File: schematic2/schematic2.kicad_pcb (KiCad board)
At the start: 2 copper layers, 69.2 x 56 mm, 36 parts, among them J1 Barrel_Jack, K1 TIANBO_HJR_1-2C, P1 Conn_02x20_Odd_Even, Q1 BC547, Q2 BC557, Q3 BC547, Q4 BC547, U1 buck

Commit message: modified:   schematic2/schematic2.kicad_pcb new file:   schematic2/schematic2.pro modified:   schematic2/schematic2.sch
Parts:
- added J2: I2C BUS, Connector_Molex:Molex_KK-254_AE-6410-05A_1x05_P2.54mm_Vertical, F.Cu at (218.5, 103.2)
- added REF**: KiCad-Logo_6mm_SilkScreen, Symbol:KiCad-Logo_6mm_SilkScreen, F.Cu at (262.0, 133.5)
- BT1: value 6x AA NiMh -> 6x AAA NiMh
- D11: value LED -> PWR
- D8: value LED -> PWR_FAIL
- R3: value 82R -> 120R
- moved D11 27.7 mm to (206.2, 131.5), turned to 90 degrees
- moved R11 15.6 mm to (206.2, 126.2), turned to 90 degrees
- moved U1 8.50 mm to (259.2, 114.0)
- moved K1 7.75 mm to (228.2, 112.8)
- moved R9 4.50 mm to (223.5, 107.2)
- moved R10 4.25 mm to (223.5, 109.5)
- moved Q4 4.03 mm to (214.0, 110.5)
- moved J1 0.50 mm to (252.5, 135.8)
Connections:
- D10 pad 2: +3V3 -> PI_P_SIG
- P1 pad 1: (no net) -> Net-(J2-Pad5)
- P1 pad 13: (no net) -> PI_P_SIG
- P1 pad 17: +3V3 -> (no net)
- P1 pad 3: (no net) -> /GPIO2(SDA1)
- P1 pad 5: (no net) -> /GPIO3(SCL1)
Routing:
- net PI_P_SIG: track 0.00 -> 16.2 mm
- net +5V: track 90.0 -> 105.1 mm
- net +3V3: track 10.6 -> 0.00 mm
- net Net-(D9-Pad2): track 10.2 -> 15.4 mm
- net Net-(D7-Pad1): track 29.9 -> 35.0 mm
- net Net-(J2-Pad5): track 0.00 -> 4.49 mm
- net GND: track 0.00 -> 4.49 mm
- net /GPIO3(SCL1): track 0.00 -> 4.49 mm
- net /GPIO2(SDA1): track 0.00 -> 4.49 mm
- net Net-(D5-Pad1): track 12.5 -> 16.5 mm
- net Net-(D11-Pad2): track 6.00 -> 2.75 mm
- net Net-(D10-Pad1): track 8.08 -> 10.3 mm
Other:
- board size 69.2 x 56 mm -> 68.8 x 56 mm
- board text added: "(C) Mike Evans 2018"
- board text added: "+"
- board text removed: "RASPBERRY-PI 40-PIN ADDON BOARD VIEW FROM TOP NOTE: P1 SHOULD BE FITTED ON THE REVERSE OF THE BOARD ADD EDGE CUTS FROM CAMERA AND DISPLAY PORTS AS REQUIRED"

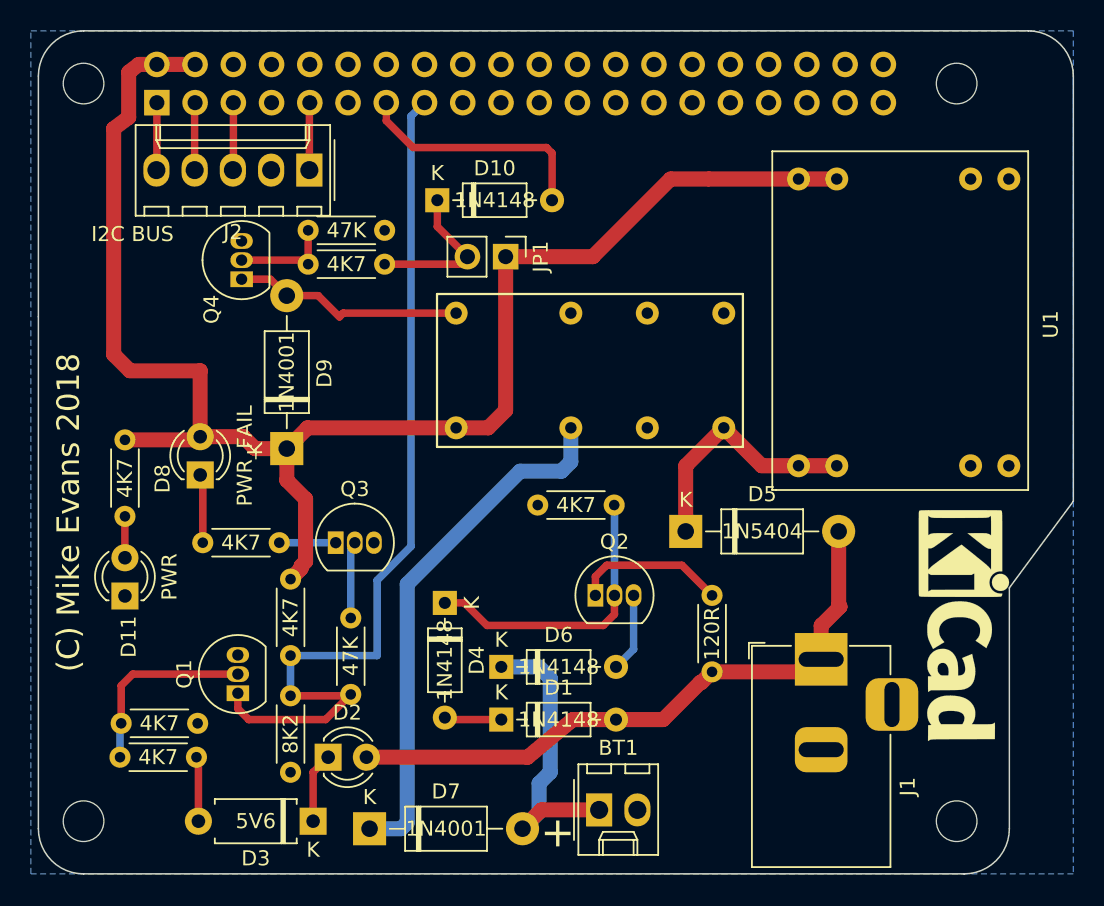
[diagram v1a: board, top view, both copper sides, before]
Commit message: add fuse and logo.
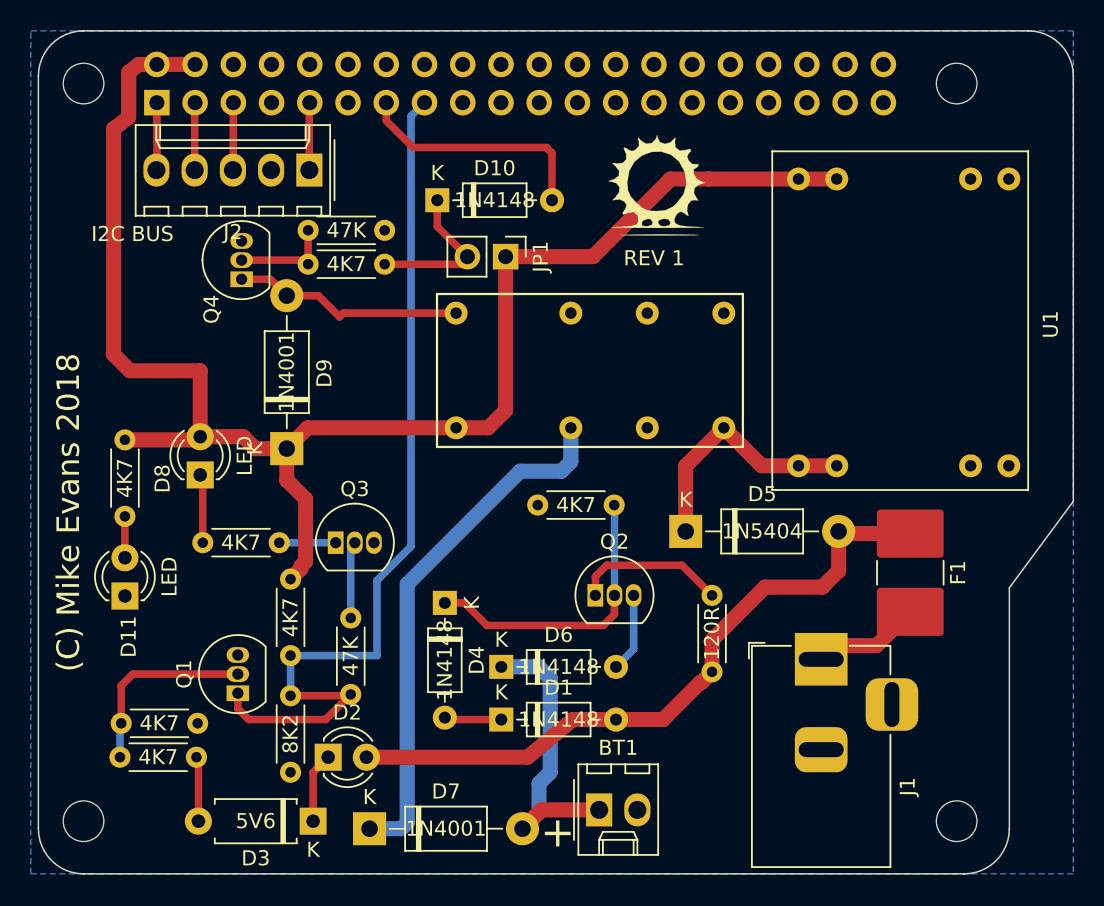
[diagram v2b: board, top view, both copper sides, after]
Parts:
- removed REF**: KiCad-Logo_6mm_SilkScreen, Symbol:KiCad-Logo_6mm_SilkScreen
- added F1: Polyfuse, Fuse:Fuse_2816_7142Metric_Pad3.20x4.45mm_HandSolder, F.Cu at (258.4, 130.0)
- added G***: LOGO, Mikee:MS_LOGO, F.Cu at (241.7, 104.3)
- D11: value PWR -> LED
- D8: value PWR_FAIL -> LED
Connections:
- J1 pad 1: +9V -> Net-(F1-Pad2)
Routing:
- net Net-(F1-Pad2): track 0.00 -> 7.76 mm
- net +9V: track 42.1 -> 45.0 mm
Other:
- board text added: "REV 1"

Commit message: Change clock for discreets.
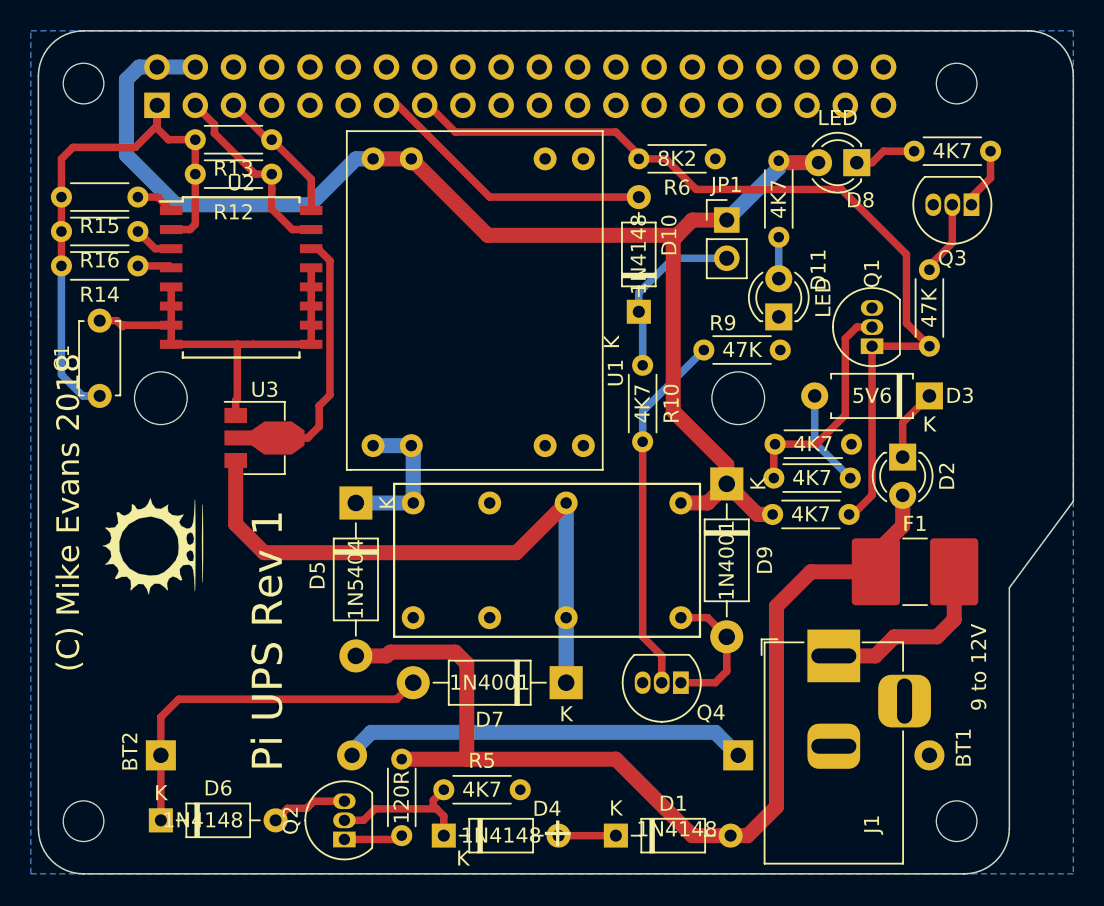
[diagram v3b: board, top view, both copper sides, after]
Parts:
- removed J2: I2C BUS, Connector_Molex:Molex_KK-254_AE-6410-05A_1x05_P2.54mm_Vertical
- added BT2: 3x AAA NiMh, Battery:BatteryHolder_Keystone_2479_3xAAA, F.Cu at (208.6, 142.1)
- added C1: C_Small, Capacitor_THT:C_Disc_D4.7mm_W2.5mm_P5.00mm, F.Cu at (204.6, 118.2)
- added R12: 4K7, Resistor_THT:R_Axial_DIN0204_L3.6mm_D1.6mm_P5.08mm_Horizontal, F.Cu at (216.0, 103.5)
- added R13: 4K7, Resistor_THT:R_Axial_DIN0204_L3.6mm_D1.6mm_P5.08mm_Horizontal, F.Cu at (216.0, 101.2)
- added R14: 4K7, Resistor_THT:R_Axial_DIN0204_L3.6mm_D1.6mm_P5.08mm_Horizontal, F.Cu at (207.1, 109.6)
- added R15: 4K7, Resistor_THT:R_Axial_DIN0204_L3.6mm_D1.6mm_P5.08mm_Horizontal, F.Cu at (207.1, 105.0)
- added R16: 4K7, Resistor_THT:R_Axial_DIN0204_L3.6mm_D1.6mm_P5.08mm_Horizontal, F.Cu at (207.1, 107.3)
- added U2: DS3231M, Package_SO:SOIC-16W_7.5x10.3mm_P1.27mm, F.Cu at (214.0, 110.4)
- added U3: MCP1700-1202E_SOT89, Package_TO_SOT_SMD:SOT-89-3, F.Cu at (215.1, 121.0)
- BT1: value 6x AAA NiMh -> 3x AAA NiMh; footprint Connector_Molex:Molex_KK-254_AE-6410-02A_1x02_P2.54mm_Vertical -> Battery:BatteryHolder_Keystone_2479_3xAAA
- moved R8 53.9 mm to (263.8, 102.0)
- moved D3 49.7 mm to (259.7, 118.2)
- moved R6 49.6 mm to (245.5, 102.5), turned to 180 degrees
- moved D8 48.3 mm to (254.9, 102.8), turned to 180 degrees
- moved Q1 48.0 mm to (255.9, 114.9)
- moved Q3 47.8 mm to (262.5, 105.5), turned to 180 degrees
- moved D11 47.2 mm to (249.7, 113.0)
- moved R1 47.2 mm to (254.4, 123.7)
- moved R11 47.2 mm to (249.7, 107.7)
- moved R2 47.2 mm to (249.4, 121.5)
- moved R7 44.9 mm to (259.7, 109.9)
- moved D2 43.1 mm to (257.9, 122.3), turned to 270 degrees
- moved G*** 41.2 mm to (208.1, 128.2), turned to 90 degrees
- moved Q4 39.6 mm to (243.2, 137.3), turned to 180 degrees
- moved R4 38.3 mm to (254.4, 126.1), turned to 180 degrees
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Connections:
- D6 pad 1: Net-(BT1-Pad1) -> Net-(BT2-Pad1)
- D7 pad 2: Net-(BT1-Pad1) -> Net-(BT2-Pad1)
- K1 pad 4: (no net) -> Net-(D7-Pad1)
- P1 pad 1: Net-(J2-Pad5) -> +3V3
- P1 pad 3: /GPIO2(SDA1) -> SDA1
- P1 pad 5: /GPIO3(SCL1) -> SCL1
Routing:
- net +3V3: track 0.00 -> 37.9 mm
- net Net-(BT2-Pad1): track 0.00 -> 24.6 mm
- net +9V: track 45.0 -> 68.6 mm
- net GND: track 4.49 -> 27.9 mm
- net Net-(U2-Pad14): track 0.00 -> 18.6 mm
- net Net-(Q4-Pad2): track 6.78 -> 24.3 mm
- net +5V: track 105.1 -> 88.6 mm
- net SDA1: track 0.00 -> 12.9 mm
- net Net-(D4-Pad1): track 19.5 -> 10.1 mm
- net SCL1: track 0.00 -> 9.33 mm
- net Net-(BT1-Pad1): track 19.9 -> 27.1 mm
- net Net-(D5-Pad1): track 16.5 -> 10.2 mm
- net Net-(Q2-Pad1): track 10.1 -> 3.92 mm
- net Net-(D9-Pad2): track 15.4 -> 9.22 mm
- net Net-(D7-Pad1): track 35.0 -> 40.3 mm
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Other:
- board text added: "9 to 12V"
- board text added: "Pi UPS Rev 1"
- board text removed: "REV 1"

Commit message: Layout done.
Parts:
- added C2: CP, Capacitor_THT:C_Disc_D4.7mm_W2.5mm_P5.00mm, F.Cu at (225.4, 120.7)
- added C3: C_Small, Capacitor_THT:C_Disc_D4.7mm_W2.5mm_P5.00mm, F.Cu at (233.4, 108.0)
- added C4: CP, Capacitor_THT:C_Disc_D4.7mm_W2.5mm_P5.00mm, F.Cu at (237.1, 107.8)
- added D12: D_Zener, Diode_THT:D_DO-35_SOD27_P7.62mm_Horizontal, F.Cu at (230.7, 122.6)
- added L1: INDUCTOR, Inductor_SMD:L_7.3x7.3_H3.5, F.Cu at (234.3, 117.2)
- added R17: R, Resistor_THT:R_Axial_DIN0204_L3.6mm_D1.6mm_P5.08mm_Horizontal, F.Cu at (221.8, 111.6)
- added R18: R, Resistor_THT:R_Axial_DIN0204_L3.6mm_D1.6mm_P5.08mm_Horizontal, F.Cu at (224.6, 104.8)
- added R19: R, Resistor_THT:R_Axial_DIN0204_L3.6mm_D1.6mm_P5.08mm_Horizontal, F.Cu at (237.3, 111.9)
- U1: value buck -> MC34063AD; footprint Mikee:BUCK_MODULE_5V -> Package_SO:SOIC-8_3.9x4.9mm_P1.27mm
- moved U1 5.24 mm to (226.9, 109.4), turned to 180 degrees
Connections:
- D5 pad 1: Net-(D5-Pad1) -> /Sheet5B480DB4/Vin
- K1 pad 9: Net-(D5-Pad1) -> /Sheet5B480DB4/Vin
- U1 pad 1: Net-(D5-Pad1) -> Net-(R17-Pad1)
- U1 pad 2: GND -> Net-(D12-Pad1)
- U1 pad 3: GND -> Net-(C3-Pad1)
- U1 pad 4: +5V -> GND
- U3 pad 3: Net-(D7-Pad1) -> (no net)
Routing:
- net /Sheet5B480DB4/Vin: track 0.00 -> 28.0 mm
- net Net-(R17-Pad1): track 0.00 -> 27.6 mm
- net Net-(D12-Pad1): track 0.00 -> 18.2 mm
- net Net-(R18-Pad1): track 0.00 -> 15.7 mm
- net +5V: track 88.6 -> 99.5 mm
- net Net-(D5-Pad1): track 10.2 -> 0.00 mm
- net Net-(D7-Pad1): track 40.3 -> 36.0 mm
- net Net-(C3-Pad1): track 0.00 -> 4.09 mm
- net GND: track 27.9 -> 30.1 mm

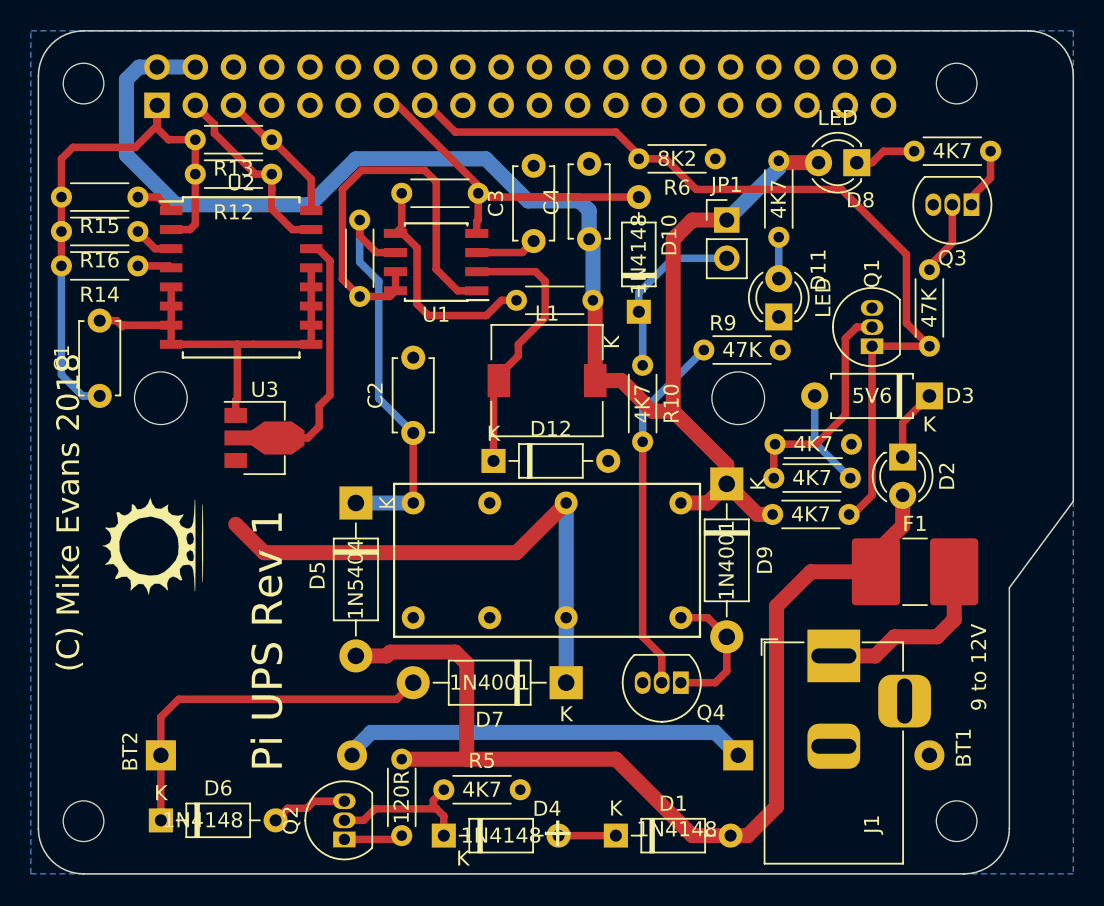
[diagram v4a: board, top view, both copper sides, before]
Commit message: Put the prebuilt buck converter back.
It's cheaper and easier.
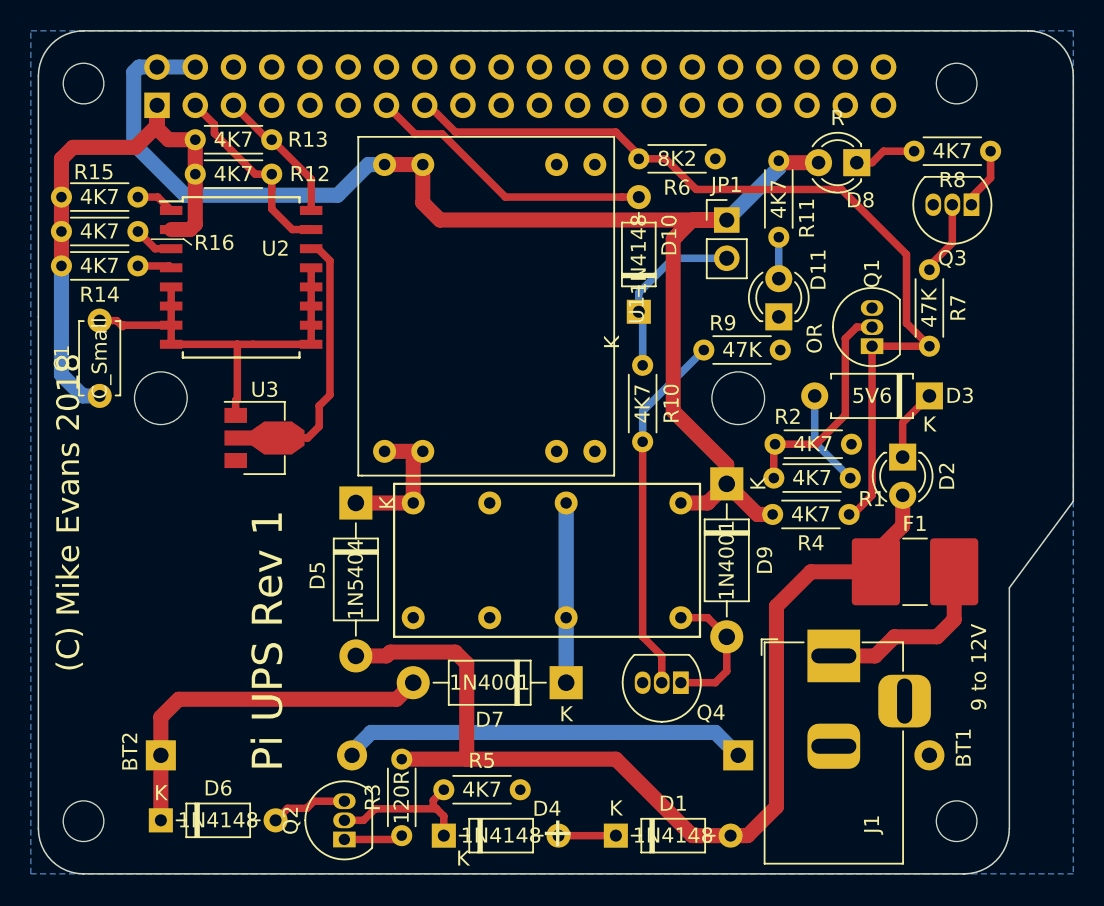
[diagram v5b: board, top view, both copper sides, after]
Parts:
- removed C2, C4: CP, Capacitor_THT:C_Disc_D4.7mm_W2.5mm_P5.00mm
- removed C3: C_Small, Capacitor_THT:C_Disc_D4.7mm_W2.5mm_P5.00mm
- removed D12: D_Zener, Diode_THT:D_DO-35_SOD27_P7.62mm_Horizontal
- removed G***: LOGO, Mikee:MS_LOGO
- removed L1: INDUCTOR, Inductor_SMD:L_7.3x7.3_H3.5
- removed R17, R18, R19: R, Resistor_THT:R_Axial_DIN0204_L3.6mm_D1.6mm_P5.08mm_Horizontal
- D11: value LED -> OR
- D2: value LED -> G
- D8: value LED -> R
- U1: value MC34063AD -> buck; footprint Package_SO:SOIC-8_3.9x4.9mm_P1.27mm -> Mikee:BUCK_MODULE_5V
- moved U1 6.07 mm to (231.8, 113.0), turned to 90 degrees
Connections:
- D5 pad 1: /Sheet5B480DB4/Vin -> Net-(D5-Pad1)
- K1 pad 11: (no net) -> Net-(K1-Pad11)
- K1 pad 6: (no net) -> Net-(K1-Pad6)
- K1 pad 8: (no net) -> Net-(K1-Pad8)
- K1 pad 9: /Sheet5B480DB4/Vin -> Net-(D5-Pad1)
- P1 pad 10: (no net) -> /GPIO15(RXD0)
- P1 pad 11: (no net) -> /GPIO17(GEN0)
- P1 pad 12: (no net) -> /GPIO18(GEN1)(PWM0)
- P1 pad 16: (no net) -> /GPIO23(GEN4)
- P1 pad 17: (no net) -> Net-(P1-Pad17)
- P1 pad 18: (no net) -> /GPIO24(GEN5)
- P1 pad 19: (no net) -> /GPIO10(SPI0_MOSI)
- P1 pad 21: (no net) -> /GPIO9(SPI0_MISO)
- P1 pad 22: (no net) -> /GPIO25(GEN6)
- P1 pad 23: (no net) -> /GPIO11(SPI0_SCK)
- P1 pad 24: (no net) -> /GPIO8(SPI0_CE_N)
- P1 pad 26: (no net) -> /GPIO7(SPI1_CE_N)
- P1 pad 27: (no net) -> /ID_SD
- P1 pad 28: (no net) -> /ID_SC
- P1 pad 29: (no net) -> /GPIO5
- P1 pad 31: (no net) -> /GPIO6
- P1 pad 32: (no net) -> /GPIO12(PWM0)
- P1 pad 33: (no net) -> /GPIO13(PWM1)
- P1 pad 35: (no net) -> /GPIO19(SPI1_MISO)
- P1 pad 36: (no net) -> /GPIO16
- P1 pad 37: (no net) -> /GPIO26
- P1 pad 38: (no net) -> /GPIO20(SPI1_MOSI)
- P1 pad 40: (no net) -> /GPIO21(SPI1_SCK)
- P1 pad 7: (no net) -> /GPIO4(GCLK)
- P1 pad 8: (no net) -> /GPIO14(TXD0)
- U1 pad 1: Net-(R17-Pad1) -> Net-(D5-Pad1)
- U1 pad 2: Net-(D12-Pad1) -> GND
- U1 pad 3: Net-(C3-Pad1) -> GND
- U1 pad 4: GND -> +5V
- U3 pad 3: (no net) -> /Sheet5B4BA297/V0
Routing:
- net /Sheet5B480DB4/Vin: track 28.0 -> 0.00 mm
- net Net-(R17-Pad1): track 27.6 -> 0.00 mm
- net Net-(D7-Pad1): track 36.0 -> 11.9 mm
- net Net-(D12-Pad1): track 18.2 -> 0.00 mm
- net Net-(R18-Pad1): track 15.7 -> 0.00 mm
- net Net-(D5-Pad1): track 0.00 -> 10.0 mm
- net +5V: track 99.5 -> 90.4 mm
- net Net-(C3-Pad1): track 4.09 -> 0.00 mm
- net GND: track 30.1 -> 27.9 mm
